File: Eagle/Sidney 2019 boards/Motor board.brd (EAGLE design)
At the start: 110 x 122 mm, 39 parts, among them IC1 LM2596S, IC2 LM2940CS-5.0_NOPB

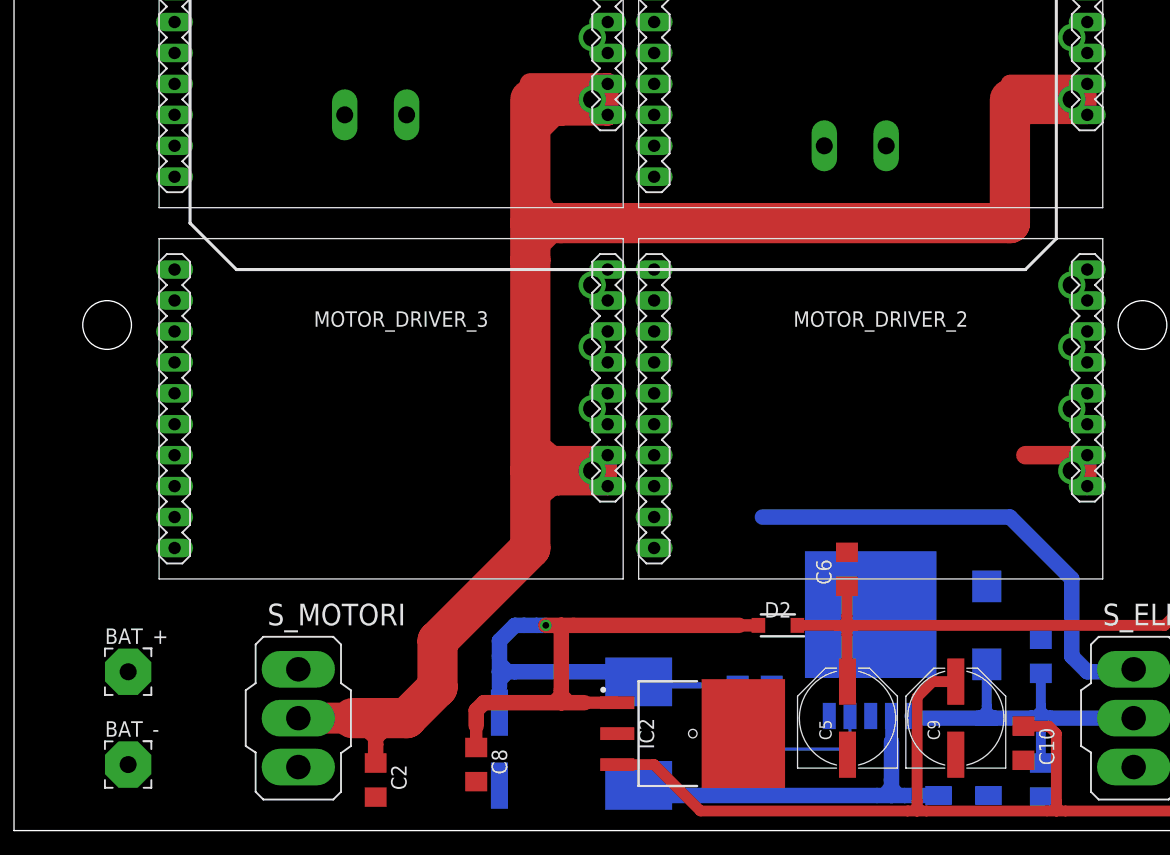
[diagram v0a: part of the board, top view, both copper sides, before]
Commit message: Finished components lists for both boards and fixed line sensors' connectors pinout
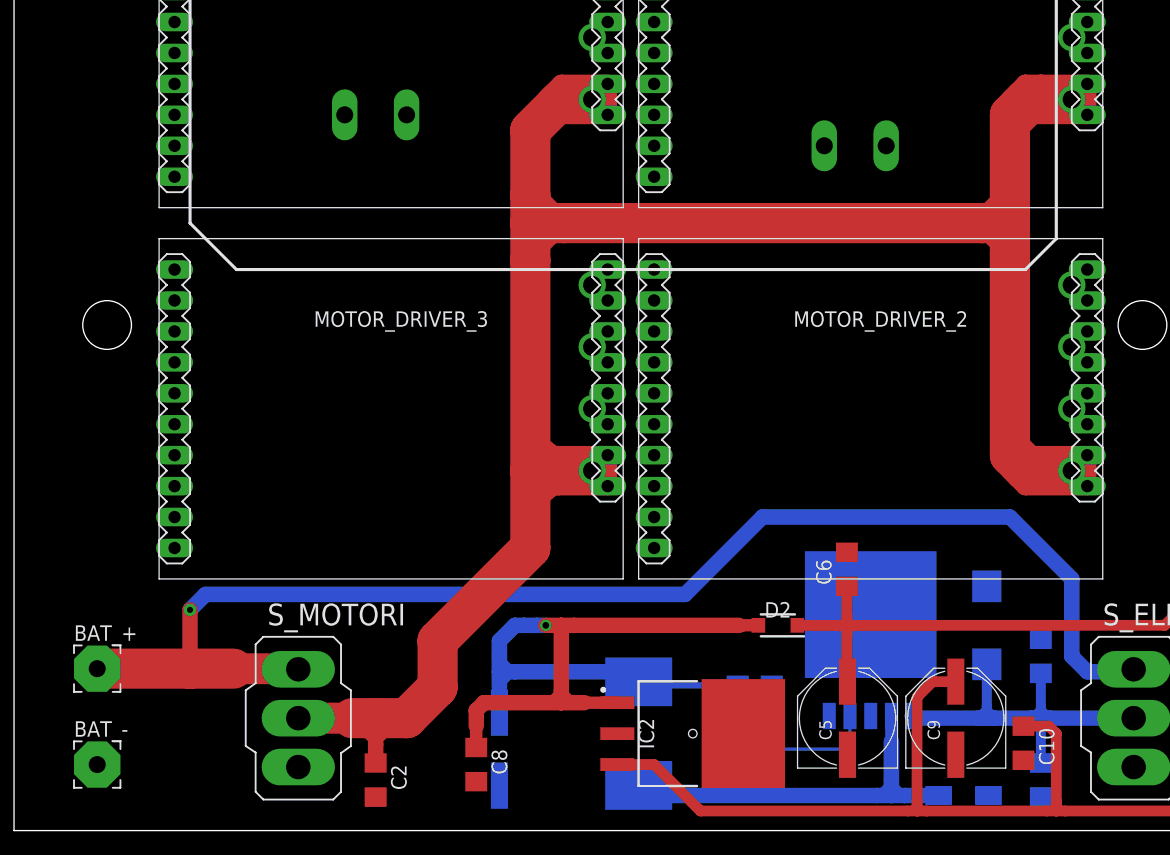
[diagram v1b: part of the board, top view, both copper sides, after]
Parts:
- moved BAT_+ 2.55 mm to (36.8, 66.3)
- moved BAT_- 2.54 mm to (36.8, 58.4)
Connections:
- removed net S1_DOWN: S1.2, SIGN_CON.19
- removed net S1_UP: S1.1, SIGN_CON.20
- removed net S2_DOWN: S2.2, SIGN_CON.15
- removed net S2_UP: S2.1, SIGN_CON.17
- removed net S3_DOWN: S3.2, SIGN_CON.11
- removed net S3_UP: S3.1, SIGN_CON.13
- removed net S4_DOWN: S4.2, SIGN_CON.7
- removed net S4_UP: S4.1, SIGN_CON.9
- new net S1_IN: S1.2, SIGN_CON.20
- new net S1_OUT: S1.3, SIGN_CON.19
- new net S2_IN: S2.2, SIGN_CON.17
- new net S2_OUT: S2.3, SIGN_CON.15
- new net S3_IN: S3.2, SIGN_CON.13
- new net S3_OUT: S3.3, SIGN_CON.11
- new net S4_IN: S4.2, SIGN_CON.9
- new net S4_OUT: S4.3, SIGN_CON.7
- net +5V/S: now also S1.1, S2.1, S3.1, S4.1; no longer S1.3, S2.3, S3.3, S4.3
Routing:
- net N$1: track 39.5 -> 111.0 mm, vias 0 -> 1
- net VMOT: track 203.5 -> 250.6 mm

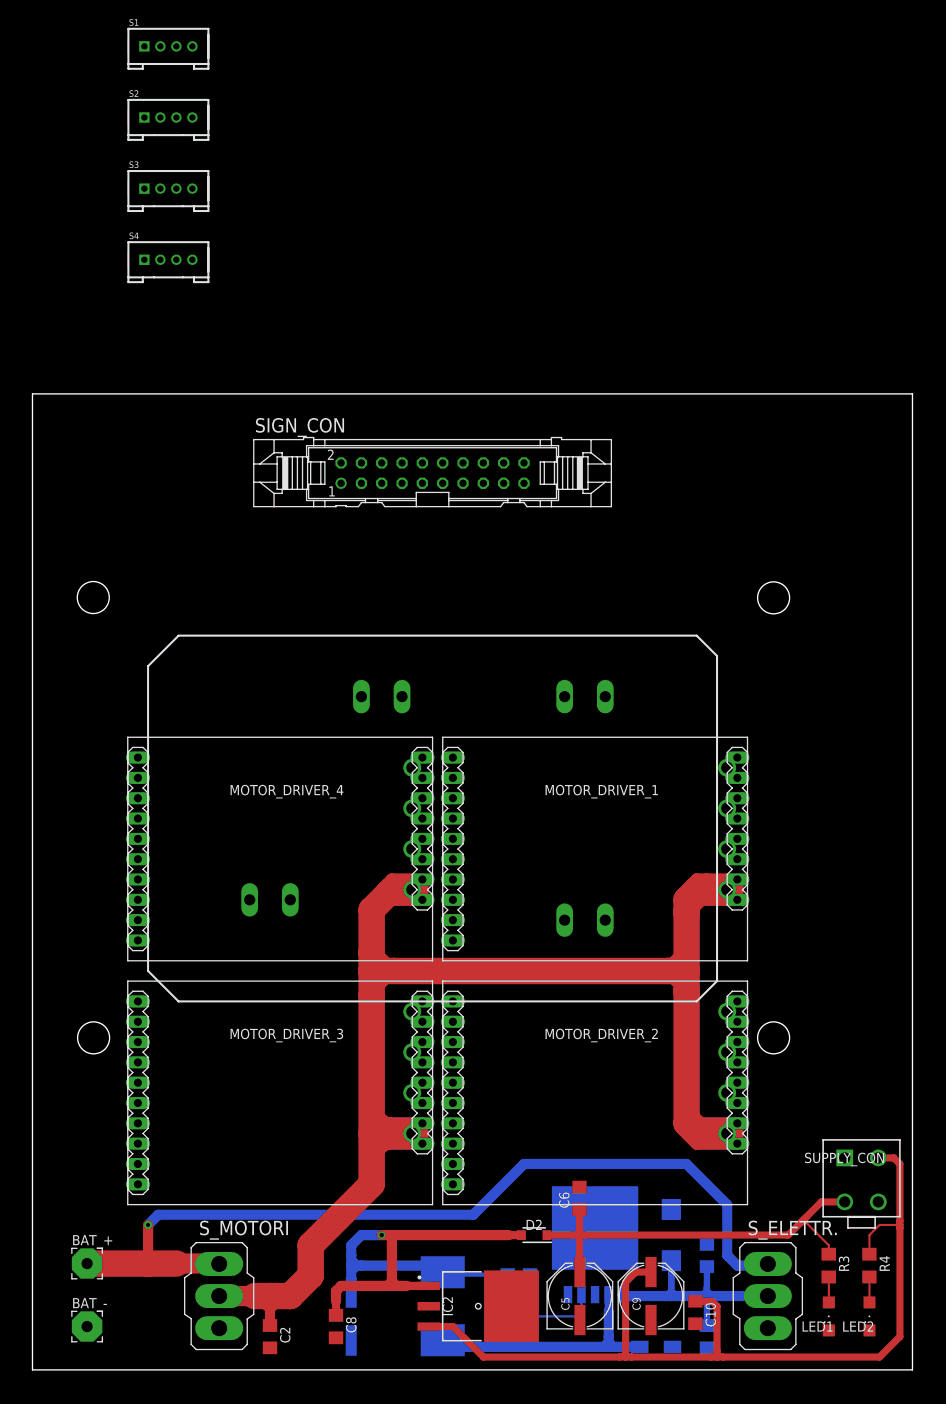
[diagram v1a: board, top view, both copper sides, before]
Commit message: Finished motor board, deleted useless files, added parts in components lists for both boards and other stuff
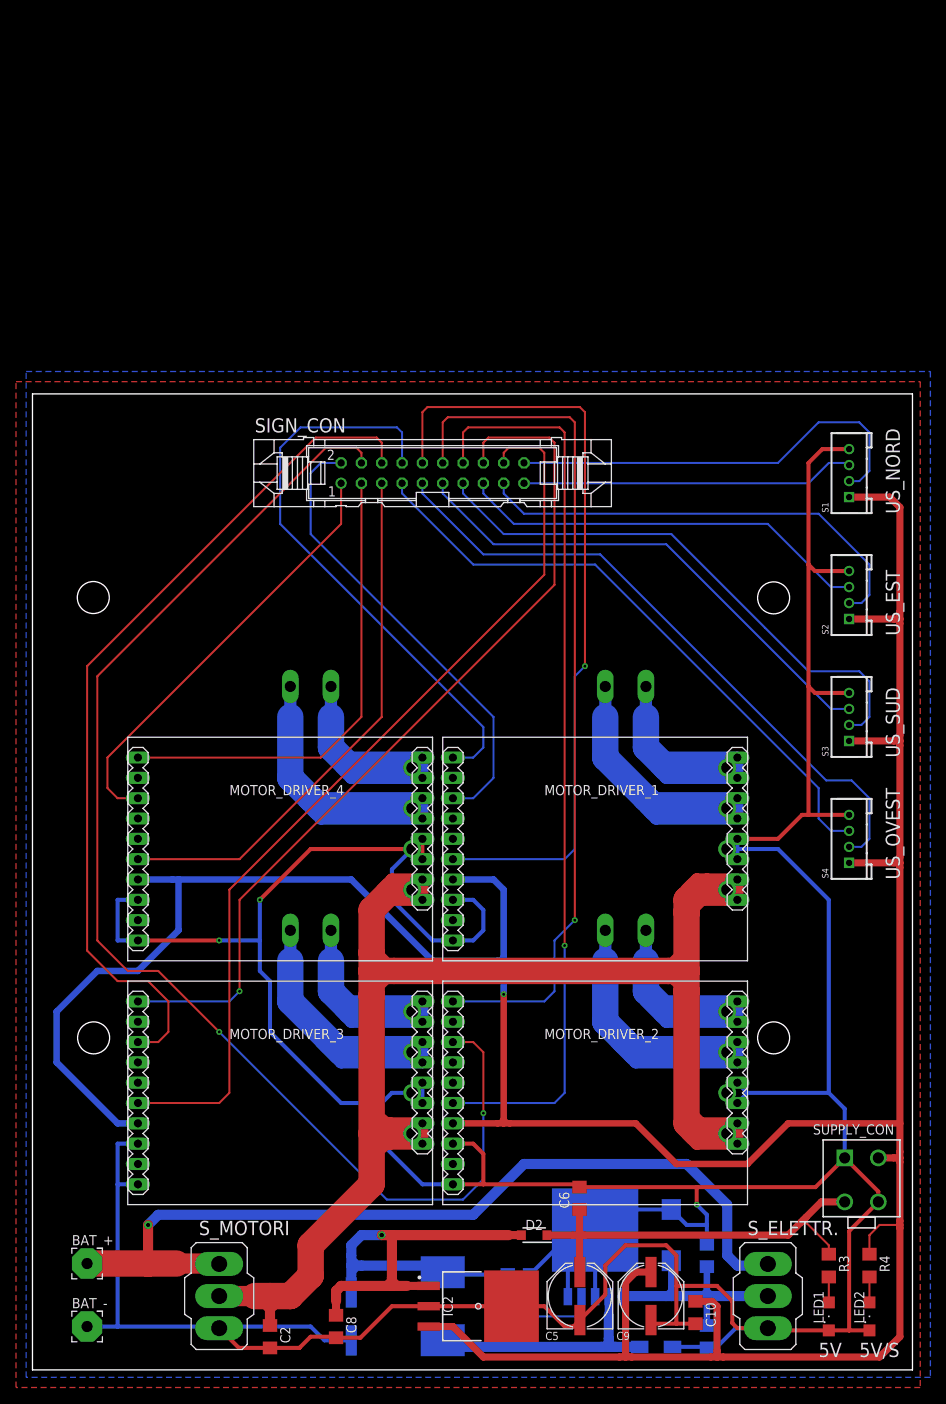
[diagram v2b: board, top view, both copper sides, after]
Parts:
- IC1: value LM2596S -> (none); device national-semiconductor:TO263-5 -> linear:TO263-5
- moved S4 111.7 mm to (132.1, 119.4), turned to 90 degrees
- moved S3 107.7 mm to (132.1, 134.6), turned to 90 degrees
- moved S2 103.9 mm to (132.1, 149.9), turned to 90 degrees
- moved S1 100.4 mm to (132.1, 165.1), turned to 90 degrees
- moved MOT_4 8.98 mm to (64.8, 138.4)
- moved MOT_3 6.35 mm to (64.8, 108.0)
- moved MOT_1 5.24 mm to (104.1, 138.4)
- moved MOT_2 5.24 mm to (104.1, 108.0)
- moved IC1 0.25 mm to (100.3, 67.9)
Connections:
- net GND: now also IC1.6
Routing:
- net GND: track 0.00 -> 611.7 mm, vias 0 -> 3
- net +5V/S: track 120.9 -> 432.5 mm, vias 0 -> 1
- net M2_PWM: track 0.00 -> 162.3 mm, vias 0 -> 2
- net M3_INB: track 0.00 -> 115.1 mm
- net M2_INB: track 0.00 -> 114.1 mm, vias 0 -> 1
- net M3_INA: track 0.00 -> 110.1 mm, vias 0 -> 1
- net M3_PWM: track 0.00 -> 108.0 mm
- net M2_INA: track 0.00 -> 107.5 mm, vias 0 -> 1
- net M1_INB: track 0.00 -> 98.1 mm, vias 0 -> 1
- net S4_IN: track 0.00 -> 81.0 mm
- net S4_OUT: track 0.00 -> 76.9 mm
- net M1_INA: track 0.00 -> 72.7 mm
- net S3_IN: track 0.00 -> 69.2 mm
- net M4_INB: track 0.00 -> 67.1 mm
- net S3_OUT: track 0.00 -> 63.2 mm
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- added copper zone on layer 1, net GND
- added copper zone on layer 16, net GND
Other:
- board text added: "5V"
- board text added: "5V/S"
- board text added: "US_EST"
- board text added: "US_NORD"
- board text added: "US_OVEST"
- board text added: "US_SUD"
